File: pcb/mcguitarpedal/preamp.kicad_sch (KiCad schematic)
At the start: 24 parts, among them J8 POT_HP_VOLUME_10k, U3 LM4562

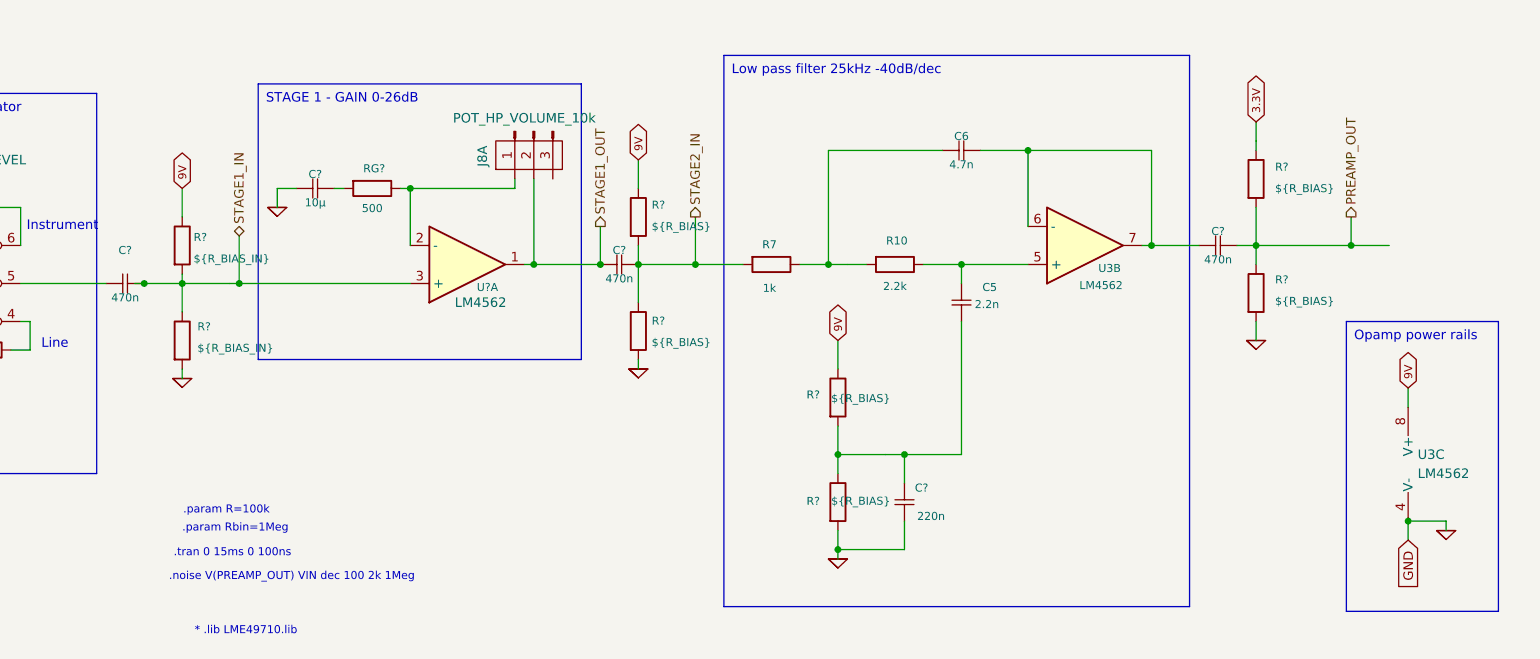
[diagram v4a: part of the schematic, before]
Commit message: Changed to DPDT switches
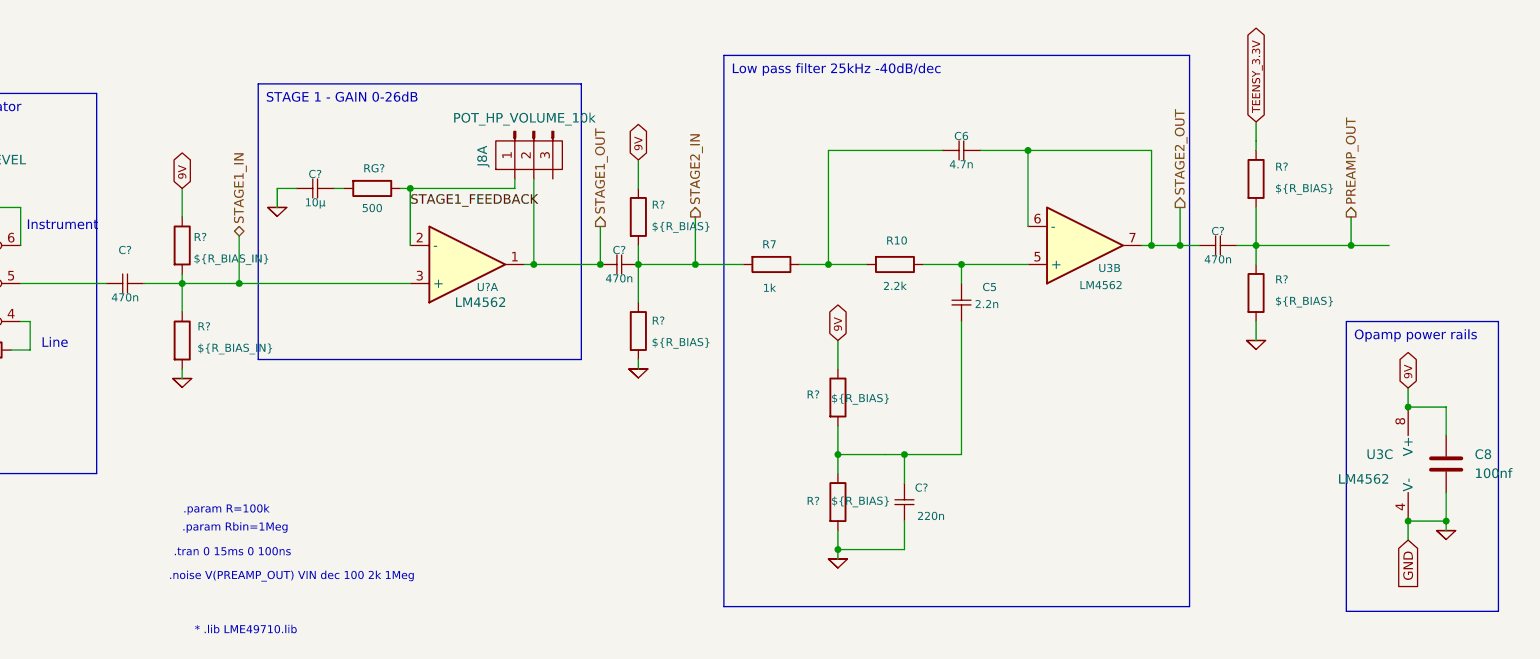
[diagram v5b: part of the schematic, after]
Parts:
- added C8: 100nf, Capacitor_THT:C_Rect_L7.2mm_W2.5mm_P5.00mm_FKS2_FKP2_MKS2_MKP2, symbol Device:C
- C? (x3): footprint Capacitor_THT:C_Rect_L18.0mm_W5.0mm_P15.00mm_FKS3_FKP3 -> Capacitor_THT:C_Rect_L7.2mm_W3.5mm_P5.00mm_FKS2_FKP2_MKS2_MKP2
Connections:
- net 0: now also C8.2
- net 9V: now also C8.1
- net STAGE1_FEEDBACK: now reaches J8.1 (Pin_1), RG?.1, U?.2 (-)
- net STAGE2_OUT: now reaches C6.1, C?.2, U3.6 (-), U3.7
- net 3.3V renamed TEENSY_3.3V
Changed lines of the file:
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@@
 	)
 	(junction
+		(at 233.68 120.65)
+		(diameter 0)
+		(color 0 0 0 0)
+	)
+	(junction
 		(at 138.43 101.6)
 		(diameter 0)
@@
 	)
 	(junction
+		(at 238.76 135.89)
+		(diameter 0)
+		(color 0 0 0 0)
+	)
+	(junction
 		(at 157.48 139.7)
 		(diameter 0)
@@
 	)
 	(junction
-		(at 64.77 104.14)
+		(at 203.2 99.06)
 		(diameter 0)
 		(color 0 0 0 0)
@@
 	(wire
 		(pts
-			(xy 100.33 91.44) (xy 114.3 91.44)
-		)
-		(stroke
-			(width 0)
-			(type default)
-		)
-	)
-	(wire
-		(pts
 			(xy 38.1 113.03) (xy 38.1 109.22)
 		)
@@
 	(wire
 		(pts
-			(xy 63.5 104.14) (xy 64.77 104.14)
-		)
-		(stroke
-			(width 0.1524)
-			(type solid)
-		)
-	)
-	(wire
-		(pts
 			(xy 173.99 127) (xy 173.99 109.22)
 		)
@@
 	(wire
 		(pts
+			(xy 100.33 91.44) (xy 114.3 91.44)
+		)
+		(stroke
+			(width 0)
+			(type default)
+		)
+	)
+	(wire
+		(pts
 			(xy 22.86 104.14) (xy 38.1 104.14)
 		)
@@
 	(wire
 		(pts
+			(xy 203.2 99.06) (xy 205.74 99.06)
+		)
+		(stroke
+			(width 0.1524)
+			(type solid)
+		)
+	)
+	(wire
+		(pts
 			(xy 69.85 91.44) (xy 69.85 95.25)
 		)
@@
 	(wire
 		(pts
+			(xy 238.76 132.08) (xy 238.76 135.89)
+		)
+		(stroke
+			(width 0)
+			(type default)
+		)
+	)
+	(wire
+		(pts
 			(xy 48.26 99.06) (xy 48.26 93.98)
 		)
@@
 	(wire
 		(pts
+			(xy 238.76 120.65) (xy 233.68 120.65)
+		)
+		(stroke
+			(width 0)
+			(type default)
+		)
+	)
+	(wire
+		(pts
 			(xy 38.1 93.98) (xy 48.26 93.98)
 		)
@@
 	(wire
 		(pts
+			(xy 203.2 93.98) (xy 203.2 99.06)
+		)
+		(stroke
+			(width 0.1524)
+			(type solid)
+		)
+	)
+	(wire
+		(pts
 			(xy 213.36 101.6) (xy 213.36 99.06)
 		)
@@
 	(wire
 		(pts
-			(xy 199.39 99.06) (xy 205.74 99.06)
+			(xy 238.76 124.46) (xy 238.76 120.65)
+		)
+		(stroke
+			(width 0)
+			(type default)
+		)
+	)
+	(wire
+		(pts
+			(xy 199.39 99.06) (xy 203.2 99.06)
 		)
 		(stroke
@@
 		)
 	)
+	(label "STAGE1_FEEDBACK"
+		(at 100.33 93.98 0)
+		(fields_autoplaced yes)
+		(effects
+			(font
+				(size 1.27 1.27)
+			)
+			(justify left bottom)
+		)
+	)
 	(global_label "9V"
 		(shape bidirectional)
@@
 		)
 	)
-	(global_label "3.3V"
+	(global_label "TEENSY_3.3V"
 		(shape bidirectional)
 		(at 213.36 82.55 90)
@@
 		)
 	)
+	(hierarchical_label "STAGE2_OUT"
+		(shape output)
+		(at 203.2 93.98 90)
+		(fields_autoplaced yes)
+		(effects
+			(font
+				(size 1.27 1.27)
+			)
+			(justify left)
+		)
+	)
 	(hierarchical_label "STAGE1_OUT"
 		(shape output)
@@
 			)
 		)
-		(property "Footprint" "Capacitor_THT:C_Rect_L18.0mm_W5.0mm_P15.00mm_FKS3_FKP3"
+		(property "Footprint" "Capacitor_THT:C_Rect_L7.2mm_W3.5mm_P5.00mm_FKS2_FKP2_MKS2_MKP2"
 			(at 64.77 102.87 0)
 			(effects
@@
 		(on_board yes)
 		(dnp no)
-		(fields_autoplaced yes)
 		(property "Reference" "U3"
-			(at 234.95 126.9999 0)
+			(at 228.092 127 0)
 			(effects
 				(font
@@
 		)
 		(property "Value" "LM4562"
-			(at 234.95 129.5399 0)
+			(at 224.282 130.302 0)
 			(effects
 				(font
@@
 	)
 	(symbol
+		(lib_id "Device:C")
+		(at 238.76 128.27 0)
+		(unit 1)
+		(exclude_from_sim no)
+		(in_bom yes)
+		(on_board yes)
+		(dnp no)
+		(property "Reference" "C8"
+			(at 242.57 126.9999 0)
+			(effects
+				(font
+					(size 1.27 1.27)
+				)
+				(justify left)
+			)
+		)
+		(property "Value" "100nf"
+			(at 242.57 129.5399 0)
+			(effects
+				(font
+					(size 1.27 1.27)
+				)
+				(justify left)
+			)
+		)
+		(property "Footprint" "Capacitor_THT:C_Rect_L7.2mm_W2.5mm_P5.00mm_FKS2_FKP2_MKS2_MKP2"
+			(at 239.7252 132.08 0)
+			(effects
+				(font
+					(size 1.27 1.27)
+				)
+				(hide yes)
+			)
+		)
+		(property "Datasheet" "~"
+			(at 238.76 128.27 0)
+			(effects
+				(font
+					(size 1.27 1.27)
+				)
+				(hide yes)
+			)
+		)
+		(property "Description" "Unpolarized capacitor"
+			(at 238.76 128.27 0)
+			(effects
+				(font
+					(size 1.27 1.27)
+				)
+				(hide yes)
+			)
+		)
+		(pin "1"
+		)
+		(pin "2"
+		)
+		(instances
+			(project ""
+				(path "/abf63e65-3dbc-486e-8cbe-833bb40c3c0d/c177d22b-45a9-4502-a618-667d0401078d"
+					(reference "C8")
+					(unit 1)
+				)
+			)
+		)
+	)
+	(symbol
 		(lib_id "Device:R")
 		(at 213.36 90.17 0)
@@
 			)
 		)
-		(property "Footprint" "Capacitor_THT:C_Rect_L18.0mm_W5.0mm_P15.00mm_FKS3_FKP3"
+		(property "Footprint" "Capacitor_THT:C_Rect_L7.2mm_W3.5mm_P5.00mm_FKS2_FKP2_MKS2_MKP2"
 			(at 130.81 100.33 0)
 			(effects
@@
 			)
 		)
-		(property "Footprint" "Capacitor_THT:C_Rect_L18.0mm_W5.0mm_P15.00mm_FKS3_FKP3"
+		(property "Footprint" "Capacitor_THT:C_Rect_L7.2mm_W3.5mm_P5.00mm_FKS2_FKP2_MKS2_MKP2"
 			(at 210.82 97.79 0)
 			(effects

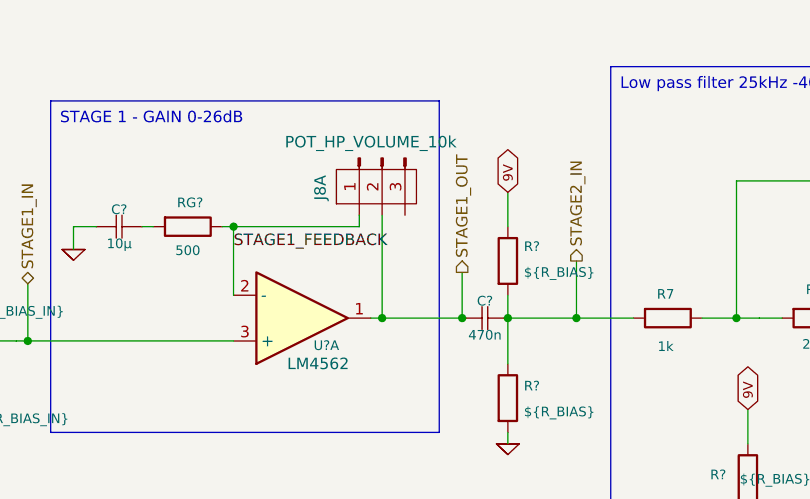
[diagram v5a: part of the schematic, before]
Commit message: HCT595, audio shield sockets
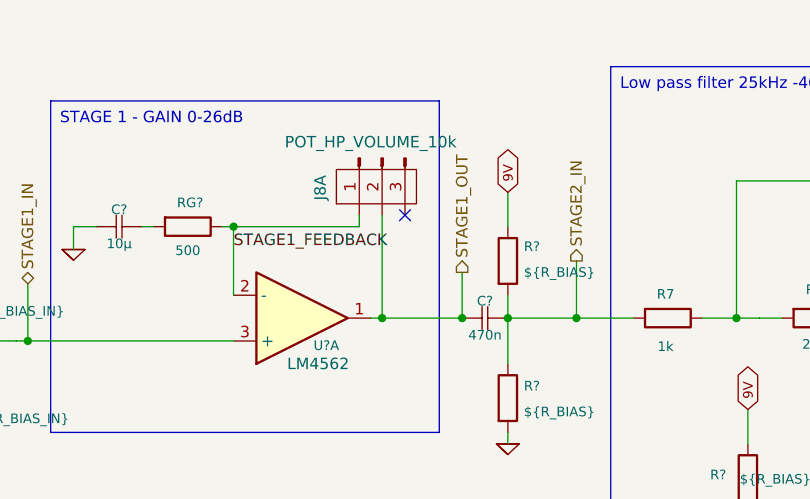
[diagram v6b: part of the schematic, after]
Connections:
- no-connect marks 0 -> 1
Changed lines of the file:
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@@
 		(color 0 0 0 0)
+	)
+	(no_connect
+		(at 119.38 90.17)
 	)
 	(wire

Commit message: Miniaturization
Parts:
- removed R?: 10k, Resistor_THT:R_Axial_DIN0207_L6.3mm_D2.5mm_P7.62mm_Horizontal, symbol Device:R
- added R1, R34, R35: 10k, Resistor_SMD:R_1206_3216Metric_Pad1.30x1.75mm_HandSolder, symbol Device:R_Small
- R?: value 4.7k -> 10k; footprint Resistor_THT:R_Axial_DIN0207_L6.3mm_D2.5mm_P7.62mm_Horizontal -> Resistor_SMD:R_1206_3216Metric_Pad1.30x1.75mm_HandSolder; symbol Device:R -> Device:R_Small
- SW?: footprint Button_Switch_THT:SW_CK_JS202011AQN_DPDT_Angled -> mcguitarpedal:DP3T slide switch; symbol Switch:SW_Slide_DPDT -> mcguitarpedal:SW_Slide_DP3T
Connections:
- net 0: now also R1.1
- net PREAMP_IN: now also SW?.7 (B), SW?.8 (C), R34.2; no longer SW?.2 (B), SW?.6 (C)
- net at SW?.3 (C): now also R?.1, R1.2; no longer R?.2
- net at SW?.4 (D): now also C?.2, SW?.2 (B); no longer R?.1
- net at SW?.5: now also R34.1, R35.2; no longer C?.2
- new net: R35.1, R?.2, SW?.6 (A)
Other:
- moved on the sheet: R?

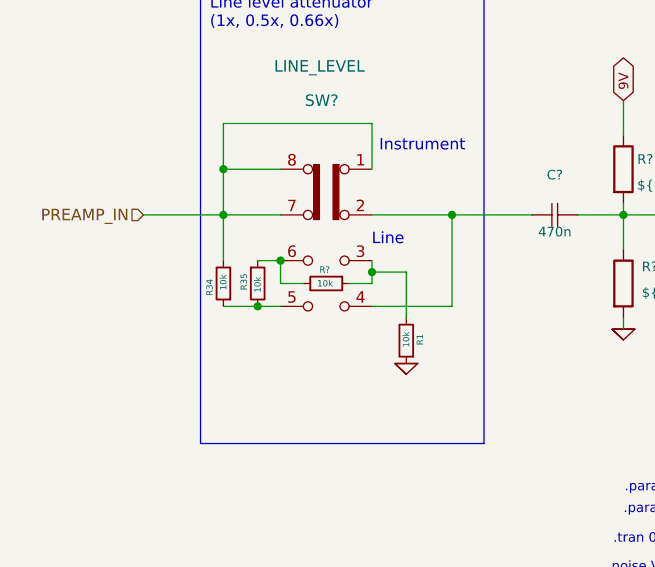
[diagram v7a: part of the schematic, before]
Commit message: Routing additonal power
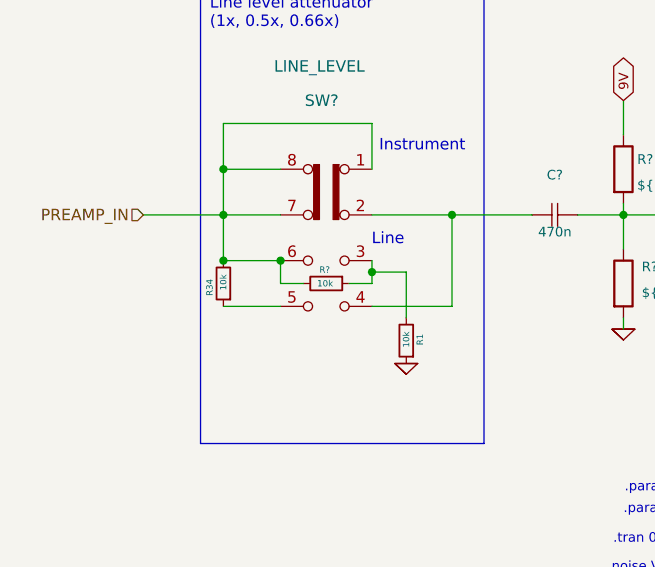
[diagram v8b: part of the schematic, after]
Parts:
- removed R35: 10k, Resistor_SMD:R_1206_3216Metric_Pad1.30x1.75mm_HandSolder, symbol Device:R_Small
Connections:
- net PREAMP_IN: now also R?.2, SW?.6 (A)
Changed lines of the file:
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@@
+	)
+	(junction
+		(at 25.4 109.22)
+		(diameter 0)
+		(color 0 0 0 0)
 	)
 	(junction
@@
 	)
 	(junction
-		(at 29.21 114.3)
-		(diameter 0)
-		(color 0 0 0 0)
-	)
-	(junction
 		(at 31.75 109.22)
 		(diameter 0)
@@
 	(wire
 		(pts
-			(xy 29.21 114.3) (xy 31.75 114.3)
-		)
-		(stroke
-			(width 0)
-			(type default)
-		)
-	)
-	(wire
-		(pts
 			(xy 100.33 91.44) (xy 100.33 99.06)
 		)
@@
 	(wire
 		(pts
-			(xy 25.4 114.3) (xy 29.21 114.3)
-		)
-		(stroke
-			(width 0)
-			(type default)
-		)
-	)
-	(wire
-		(pts
 			(xy 173.99 101.6) (xy 182.88 101.6)
 		)
@@
 	(wire
 		(pts
+			(xy 25.4 109.22) (xy 31.75 109.22)
+		)
+		(stroke
+			(width 0)
+			(type default)
+		)
+	)
+	(wire
+		(pts
 			(xy 69.85 104.14) (xy 69.85 102.87)
 		)
@@
 	(wire
 		(pts
-			(xy 29.21 109.22) (xy 31.75 109.22)
-		)
-		(stroke
-			(width 0)
-			(type default)
-		)
-	)
-	(wire
-		(pts
 			(xy 213.36 99.06) (xy 210.82 99.06)
 		)
@@
 		(pts
 			(xy 233.68 138.43) (xy 233.68 135.89)
+		)
+		(stroke
+			(width 0)
+			(type default)
+		)
+	)
+	(wire
+		(pts
+			(xy 25.4 114.3) (xy 31.75 114.3)
 		)
 		(stroke
@@
 					(unit 1)
 				)
-			)
-		)
-	)
-	(symbol
-		(lib_id "Device:R_Small")
-		(at 29.21 111.76 0)
-		(unit 1)
-		(exclude_from_sim no)
-		(in_bom yes)
-		(on_board yes)
-		(dnp no)
-		(property "Reference" "R35"
-			(at 27.686 112.522 90)
-			(effects
-				(font
-					(size 0.7 0.7)
-				)
-				(justify left)
-			)
-		)
-		(property "Value" "10k"
-			(at 29.21 112.776 90)
-			(effects
-				(font
-					(size 0.7 0.7)
-				)
-				(justify left)
-			)
-		)
-		(property "Footprint" "Resistor_SMD:R_1206_3216Metric_Pad1.30x1.75mm_HandSolder"
-			(at 29.21 111.76 0)
-			(effects
-				(font
-					(size 1.27 1.27)
-				)
-				(hide yes)
-			)
-		)
-		(property "Datasheet" "~"
-			(at 29.21 111.76 0)
-			(effects
-				(font
-					(size 1.27 1.27)
-				)
-				(hide yes)
-			)
-		)
-		(property "Description" "Resistor, small symbol"
-			(at 29.21 111.76 0)
-			(effects
-				(font
-					(size 1.27 1.27)
-				)
-				(hide yes)
-			)
-		)
-		(property "Sim.Device" "R"
-			(at 29.21 111.76 0)
-			(effects
-				(font
-					(size 1.27 1.27)
-				)
-				(hide yes)
-			)
-		)
-		(property "Sim.Params" "R=${VALUE}"
-			(at 29.21 111.76 0)
-			(effects
-				(font
-					(size 1.27 1.27)
-				)
-				(hide yes)
-			)
-		)
-		(property "Value2" ""
-			(at 29.21 111.76 0)
-			(effects
-				(font
-					(size 1.27 1.27)
-				)
-				(hide yes)
-			)
-		)
-		(pin "1"
-		)
-		(pin "2"
-		)
-		(instances
-			(project "mcguitarpedal"
-				(path "/abf63e65-3dbc-486e-8cbe-833bb40c3c0d/c177d22b-45a9-4502-a618-667d0401078d"
-					(reference "R35")
-					(unit 1)
-				)
